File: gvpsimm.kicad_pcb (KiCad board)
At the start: 4 copper layers, 97.8 x 22.2 mm, 18 parts, among them J1 SIMM64_EDGE, U1 HM514400_alt, U2 HM514400_alt, U3 HM514400_alt, U4 HM514400_alt, U5 HM514400_alt, U6 HM514400_alt, U7 HM514400_alt, U8 HM514400_alt

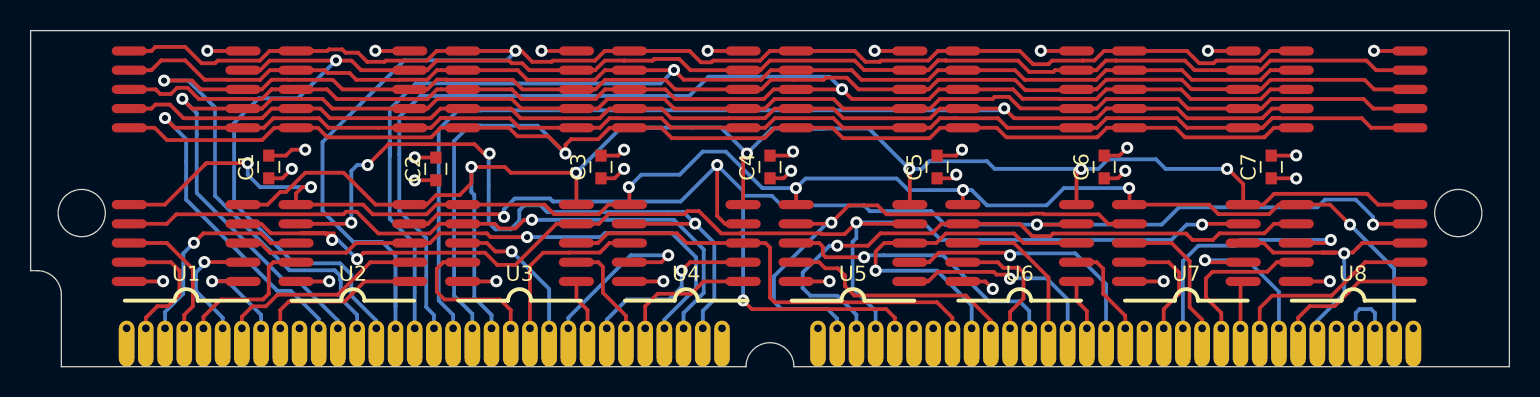
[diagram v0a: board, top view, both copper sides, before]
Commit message: Update to KiCad 8
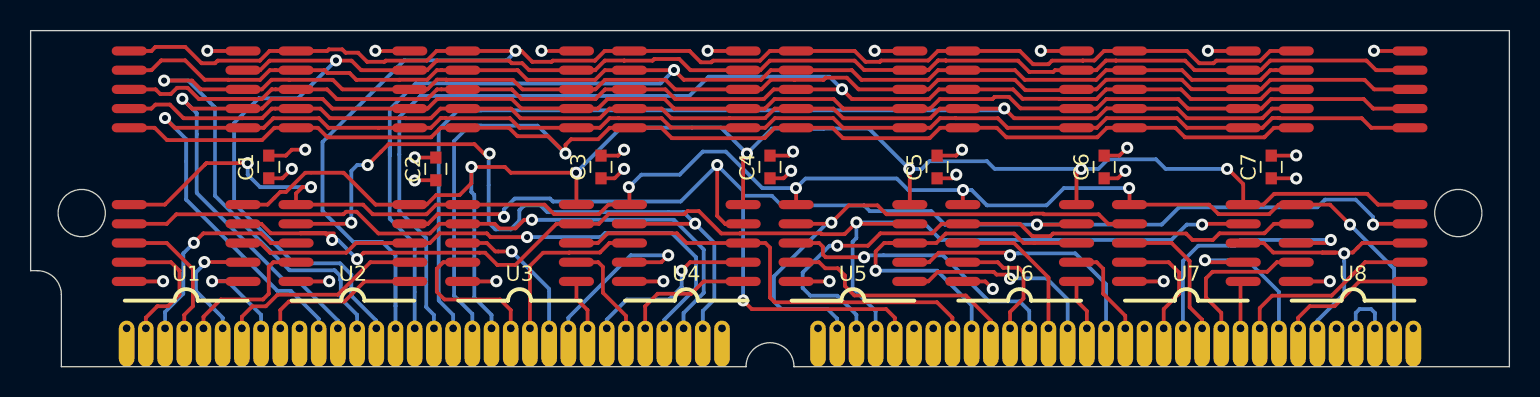
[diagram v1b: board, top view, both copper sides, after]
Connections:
- net /~CAS0 renamed /~{CAS0}
- net /~CAS1 renamed /~{CAS1}
- net /~CAS2 renamed /~{CAS2}
- net /~CAS3 renamed /~{CAS3}
- net /~OE renamed /~{OE}
- net /~RAS0 renamed /~{RAS0}
- net /~RAS1 renamed /~{RAS1}
- net /~WE0 renamed /~{WE0}
- net /~WE1 renamed /~{WE1}
- net /~WE2 renamed /~{WE2}
- net /~WE3 renamed /~{WE3}
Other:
- net class Default removed
